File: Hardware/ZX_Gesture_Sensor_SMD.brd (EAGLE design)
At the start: 57.2 x 19.1 mm, 51 parts, among them Q1 MMBT2222A, Q2 MOSFET-NCHANNEL2N7002PW, U1 PIC16F1823-14PINTSSOP, U2 MCP6021T-E/OT, U3 DMC2700UDM, U4 DMC2700UDM, U5 TSOP57238TT1

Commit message: V04 changes
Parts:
- removed U$1: GESTURESENSE_LOGOSTEXT, SparkFun-Aesthetics:GESTURESENSE_TEXT
- moved R12 13.5 mm to (40.0, 9.21), turned to 0 degrees
- moved SJ2 12.3 mm to (40.1, 11.1), turned to 90 degrees
- moved R9 11.8 mm to (40.0, 13.0), turned to 180 degrees
- moved U$5 1.50 mm to (31.9, 8.47)
- moved LOGO1 1.27 mm to (26.4, -13.7)
- moved U$6 0.90 mm to (13.7, 6.86)
- moved FID4 0.50 mm to (51.3, 17.2)
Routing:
- net GND: track 128.8 -> 165.1 mm, vias 16 -> 12
- net I2C_ADDR: track 16.4 -> 31.5 mm
- net VCC: track 105.6 -> 109.0 mm, vias 6 -> 7
- net ICSPDAT/DACOUT: track 23.0 -> 26.1 mm
- net EM2: track 37.0 -> 39.8 mm
- net RECEIVER: track 21.1 -> 23.3 mm, vias 4 -> 2
- net MCLR: track 28.8 -> 30.1 mm
- net ICSPCLK/DATA_RDY: track 30.2 -> 31.5 mm
- added copper zone on layer 1, net N$26
- added copper zone on layer 16, net N$26
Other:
- board text added: "v04"
- board text removed: "v03"

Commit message: Updated Board File
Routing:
- net I2C_SDA: track 37.1 -> 38.2 mm
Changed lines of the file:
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@@
 <setting verticaltext="up"/>
 </settings>
-<grid distance="0.025" unitdist="inch" unit="inch" style="dots" multiple="1" display="yes" altdistance="0.005" altunitdist="inch" altunit="inch"/>
+<grid distance="0.0125" unitdist="inch" unit="inch" style="dots" multiple="1" display="yes" altdistance="0.005" altunitdist="inch" altunit="inch"/>
 <layers>
 <layer number="1" name="Top" color="4" fill="1" visible="yes" active="yes"/>
-<layer number="2" name="Route2" color="1" fill="3" visible="no" active="yes"/>
-<layer number="15" name="Route15" color="4" fill="6" visible="no" active="yes"/>
+<layer number="2" name="Route2" color="1" fill="3" visible="yes" active="yes"/>
+<layer number="15" name="Route15" color="4" fill="6" visible="yes" active="yes"/>
 <layer number="16" name="Bottom" color="1" fill="1" visible="yes" active="yes"/>
 <layer number="17" name="Pads" color="2" fill="1" visible="yes" active="yes"/>
@@
 <layer number="23" name="tOrigins" color="15" fill="1" visible="yes" active="yes"/>
 <layer number="24" name="bOrigins" color="15" fill="1" visible="yes" active="yes"/>
-<layer number="25" name="tNames" color="7" fill="1" visible="no" active="yes"/>
-<layer number="26" name="bNames" color="7" fill="1" visible="no" active="yes"/>
-<layer number="27" name="tValues" color="7" fill="1" visible="no" active="yes"/>
-<layer number="28" name="bValues" color="7" fill="1" visible="no" active="yes"/>
-<layer number="29" name="tStop" color="7" fill="3" visible="no" active="yes"/>
-<layer number="30" name="bStop" color="7" fill="6" visible="no" active="yes"/>
-<layer number="31" name="tCream" color="7" fill="4" visible="no" active="yes"/>
-<layer number="32" name="bCream" color="7" fill="5" visible="no" active="yes"/>
-<layer number="39" name="tKeepout" color="4" fill="11" visible="no" active="yes"/>
-<layer number="40" name="bKeepout" color="1" fill="11" visible="no" active="yes"/>
-<layer number="41" name="tRestrict" color="4" fill="10" visible="no" active="yes"/>
-<layer number="42" name="bRestrict" color="1" fill="10" visible="no" active="yes"/>
-<layer number="43" name="vRestrict" color="2" fill="10" visible="no" active="yes"/>
-<layer number="44" name="Drills" color="7" fill="1" visible="no" active="yes"/>
+<layer number="25" name="tNames" color="7" fill="1" visible="yes" active="yes"/>
+<layer number="26" name="bNames" color="7" fill="1" visible="yes" active="yes"/>
+<layer number="27" name="tValues" color="7" fill="1" visible="yes" active="yes"/>
+<layer number="28" name="bValues" color="7" fill="1" visible="yes" active="yes"/>
+<layer number="29" name="tStop" color="7" fill="3" visible="yes" active="yes"/>
+<layer number="30" name="bStop" color="7" fill="6" visible="yes" active="yes"/>
+<layer number="31" name="tCream" color="7" fill="4" visible="yes" active="yes"/>
+<layer number="32" name="bCream" color="7" fill="5" visible="yes" active="yes"/>
+<layer number="39" name="tKeepout" color="4" fill="11" visible="yes" active="yes"/>
+<layer number="40" name="bKeepout" color="1" fill="11" visible="yes" active="yes"/>
+<layer number="41" name="tRestrict" color="4" fill="10" visible="yes" active="yes"/>
+<layer number="42" name="bRestrict" color="1" fill="10" visible="yes" active="yes"/>
+<layer number="43" name="vRestrict" color="2" fill="10" visible="yes" active="yes"/>
+<layer number="44" name="Drills" color="7" fill="1" visible="yes" active="yes"/>
 <layer number="45" name="Holes" color="7" fill="1" visible="yes" active="yes"/>
-<layer number="46" name="Milling" color="3" fill="1" visible="no" active="yes"/>
-<layer number="47" name="Measures" color="7" fill="1" visible="no" active="yes"/>
+<layer number="46" name="Milling" color="3" fill="1" visible="yes" active="yes"/>
+<layer number="47" name="Measures" color="7" fill="1" visible="yes" active="yes"/>
 <layer number="51" name="tDocu" color="6" fill="1" visible="yes" active="yes"/>
-<layer number="52" name="bDocu" color="7" fill="1" visible="no" active="yes"/>
+<layer number="52" name="bDocu" color="7" fill="1" visible="yes" active="yes"/>
 <layer number="3" name="Route3" color="4" fill="3" visible="no" active="no"/>
 <layer number="4" name="Route4" color="1" fill="4" visible="no" active="no"/>
@@
 <text x="17.3228" y="2.2479" size="1.27" layer="21" font="vector" ratio="15" align="center-right">UART</text>
 <text x="40.7797" y="2.2479" size="1.27" layer="21" font="vector" ratio="15" align="center-left">I2C</text>
-<text x="42.34815" y="11.4681" size="0.8128" layer="22" font="vector" ratio="15" rot="MR270" align="bottom-center">I2C Addr</text>
+<text x="42.545" y="11.43" size="0.8128" layer="22" font="vector" ratio="15" rot="MR270" align="bottom-center">I2C Addr</text>
 <text x="23.5839" y="16.3195" size="1.778" layer="21" font="vector" ratio="15" align="bottom-center">ZX Gesture</text>
-<text x="53.6575" y="14.4145" size="1.2192" layer="16" font="vector" ratio="15" rot="R135" align="center">v04</text>
+<text x="53.6575" y="14.4145" size="1.016" layer="16" font="vector" ratio="15" rot="R115" align="center">v04</text>
 <text x="47.0535" y="6.985" size="0.8128" layer="22" font="vector" ratio="15" rot="MR0" align="bottom-center">I2C Pullups</text>
 <text x="18.4785" y="2.3495" size="0.8128" layer="21" font="vector" ratio="15" align="bottom-center">GRN</text>
@@
 <wire x1="32.385" y1="0" x2="32.385" y2="3.175" width="0.2032" layer="21"/>
 <wire x1="32.385" y1="3.175" x2="32.385" y2="0" width="0.2032" layer="22"/>
-<text x="38.6715" y="13.49375" size="0.8128" layer="22" font="vector" ratio="15" rot="MR270">O: 0x20
+<text x="38.4175" y="13.6525" size="0.8128" layer="22" font="vector" ratio="15" rot="MR270">O: 0x20
 C: 0x22</text>
 <wire x1="11.938" y1="8.128" x2="11.938" y2="10.922" width="0.2032" layer="21"/>
@@
 <wire x1="51.91125" y1="6.73735" x2="51.9938" y2="6.6548" width="0.2032" layer="16"/>
 <wire x1="51.855" y1="8.675" x2="51.91125" y2="8.73125" width="0.2032" layer="16"/>
-<via x="28.575" y="5.715" extent="1-16" drill="0.508"/>
+<via x="28.575" y="5.715" extent="1-16" drill="0.381"/>
 <polygon width="0.2032" layer="1" isolate="0.3048">
 <vertex x="26.035" y="19.05"/>
@@
 <via x="22.5425" y="4.445" extent="1-16" drill="0.381"/>
 <via x="38.735" y="3.81" extent="1-16" drill="0.381"/>
-<wire x1="45.085" y1="3.81" x2="38.735" y2="3.81" width="0.2032" layer="16"/>
-<wire x1="45.085" y1="4.23" x2="45.085" y2="3.81" width="0.2032" layer="16"/>
 <wire x1="19.655" y1="11.3633" x2="19.655" y2="9.2375" width="0.2032" layer="16"/>
 <wire x1="23.1775" y1="8.89" x2="23.1775" y2="5.08" width="0.2032" layer="1"/>
@@
 <wire x1="38.4175" y1="4.1275" x2="38.735" y2="3.81" width="0.2032" layer="16"/>
 <wire x1="24.4475" y1="3.81" x2="33.655" y2="3.81" width="0.2032" layer="16"/>
+<wire x1="45.085" y1="4.23" x2="45.085" y2="3.175" width="0.2032" layer="16"/>
+<wire x1="45.085" y1="3.175" x2="44.7675" y2="2.8575" width="0.2032" layer="16"/>
+<wire x1="44.7675" y1="2.8575" x2="39.6875" y2="2.8575" width="0.2032" layer="16"/>
+<wire x1="39.6875" y1="2.8575" x2="38.735" y2="3.81" width="0.2032" layer="16"/>
 </signal>
 <signal name="I2C_SCL">
@@
 <wire x1="23.8125" y1="9.8425" x2="24.13" y2="9.525" width="0.2032" layer="16"/>
 <wire x1="36.068" y1="3.302" x2="36.957" y2="3.302" width="0.2032" layer="16"/>
-<wire x1="43.815" y1="4.7625" x2="38.4175" y2="4.7625" width="0.254" layer="16"/>
-<wire x1="38.4175" y1="4.7625" x2="38.1" y2="5.08" width="0.254" layer="16"/>
-<via x="38.1" y="5.08" extent="1-16" drill="0.508"/>
-<via x="37.211" y="3.048" extent="1-16" drill="0.508"/>
-<wire x1="37.211" y1="3.048" x2="37.211" y2="4.191" width="0.254" layer="1"/>
-<wire x1="37.211" y1="4.191" x2="38.1" y2="5.08" width="0.254" layer="1"/>
+<wire x1="43.815" y1="4.7625" x2="38.4175" y2="4.7625" width="0.2032" layer="16"/>
+<wire x1="38.4175" y1="4.7625" x2="38.1" y2="5.08" width="0.2032" layer="16"/>
+<via x="38.1" y="5.08" extent="1-16" drill="0.381"/>
+<via x="37.211" y="3.048" extent="1-16" drill="0.381"/>
+<wire x1="37.211" y1="3.048" x2="37.211" y2="4.191" width="0.2032" layer="1"/>
+<wire x1="37.211" y1="4.191" x2="38.1" y2="5.08" width="0.2032" layer="1"/>
 <wire x1="36.957" y1="3.302" x2="37.211" y2="3.048" width="0.2032" layer="16"/>
 <wire x1="36.195" y1="1.27" x2="36.195" y2="3.175" width="0.2032" layer="16"/>

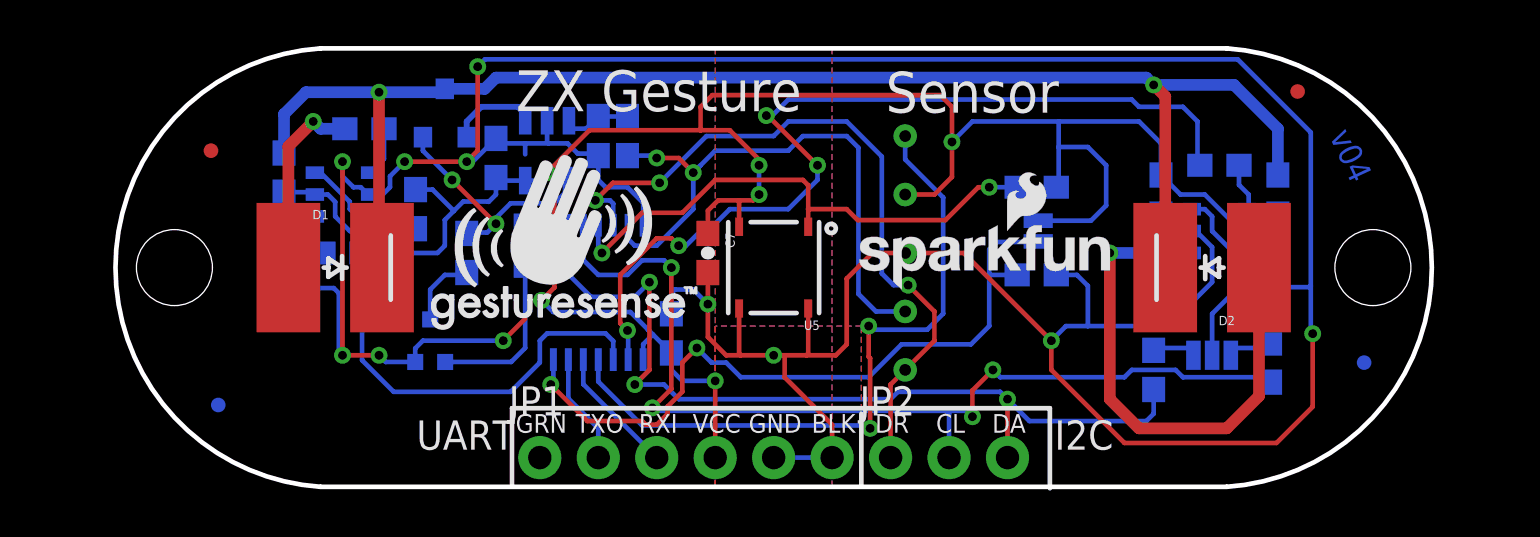
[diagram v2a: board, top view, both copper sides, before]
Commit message: Updated Brd File per Engineering Design Review
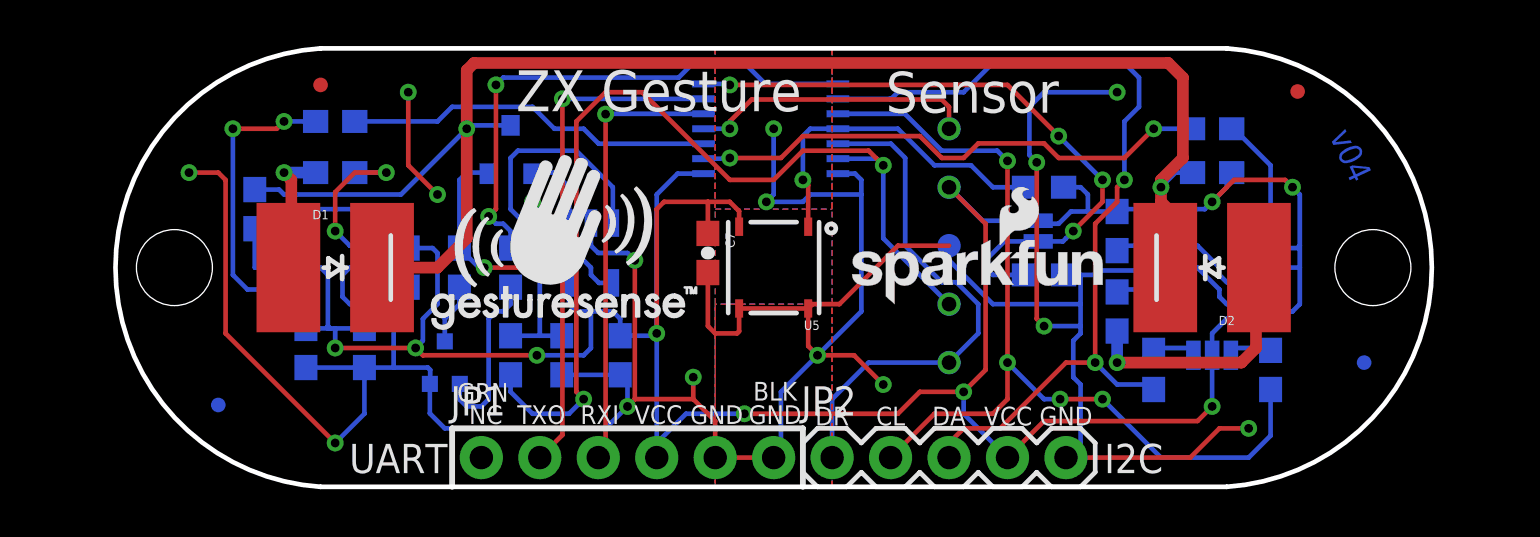
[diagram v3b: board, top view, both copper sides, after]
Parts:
- JP2: device SparkFun-Connectors:1X03_NO_SILK -> SparkFun-Connectors:1X05
- moved R1 10.8 mm to (17.1, 5.71)
- moved U1 10.3 mm to (28.4, 15.6), turned to 90 degrees
- moved C1 10.0 mm to (10.8, 6.03), turned to 270 degrees
- moved R2 9.66 mm to (19.4, 5.71)
- moved R13 5.72 mm to (9.53, 15.9)
- moved FID3 5.55 mm to (8.89, 17.5)
- moved U2 4.84 mm to (20.6, 10.2)
- moved C3 4.55 mm to (8.26, 6.03)
- moved Q1 3.27 mm to (17.1, 14.6)
- moved U3 3.19 mm to (9.53, 9.53)
- moved C6 3.01 mm to (47.6, 13.7), turned to 180 degrees
- moved R8 2.69 mm to (43.5, 7.62), turned to 270 degrees
- moved R5 2.56 mm to (12.7, 9.53)
- moved JP2 2.54 mm to (31.1, 1.27)
- moved JP1 2.54 mm to (15.9, 1.27)
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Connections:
- net GND: now also JP2.5
- net VCC: now also JP2.4
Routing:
- net VCC: track 109.0 -> 135.7 mm, vias 7 -> 10
- net CARRIER: track 1.24 -> 23.4 mm, vias 0 -> 2
- net MCLR: track 30.1 -> 12.5 mm, vias 3 -> 2
- net UART_RX: track 4.80 -> 22.1 mm, vias 0 -> 1
- net EM2: track 39.8 -> 23.1 mm, vias 4 -> 2
- net ICSPDAT/DACOUT: track 26.1 -> 42.8 mm
- net N$1: track 3.11 -> 17.3 mm
- net UART_TX: track 5.58 -> 19.3 mm, vias 0 -> 1
- net N$15: track 1.73 -> 13.6 mm, vias 0 -> 2
- net N$12: track 21.8 -> 11.3 mm
- net ICSPCLK/DATA_RDY: track 31.5 -> 22.6 mm, vias 4 -> 1
- net RECEIVER: track 23.3 -> 14.8 mm, vias 2 -> 1
- net N$8: track 5.57 -> 11.6 mm
- net N$6: track 2.16 -> 7.10 mm, vias 0 -> 2
- net N$2: track 11.2 -> 16.1 mm
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- removed copper zone on layer 1, net N$26
- removed copper zone on layer 16, net N$26
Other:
- board text added: "NC"

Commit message: Updated Brd/Sch files per QC Review
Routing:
- net GND: track 162.5 -> 163.7 mm, vias 15 -> 16
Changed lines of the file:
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@@
 <setting verticaltext="up"/>
 </settings>
-<grid distance="0.1" unitdist="inch" unit="inch" style="dots" multiple="1" display="yes" altdistance="0.005" altunitdist="inch" altunit="inch"/>
+<grid distance="0.0125" unitdist="inch" unit="inch" style="dots" multiple="1" display="yes" altdistance="0.005" altunitdist="inch" altunit="inch"/>
 <layers>
-<layer number="1" name="Top" color="4" fill="1" visible="yes" active="yes"/>
+<layer number="1" name="Top" color="4" fill="1" visible="no" active="yes"/>
 <layer number="2" name="Route2" color="1" fill="3" visible="no" active="yes"/>
 <layer number="15" name="Route15" color="4" fill="6" visible="no" active="yes"/>
@@
 <layer number="43" name="vRestrict" color="2" fill="10" visible="no" active="yes"/>
 <layer number="44" name="Drills" color="7" fill="1" visible="no" active="yes"/>
-<layer number="45" name="Holes" color="7" fill="1" visible="yes" active="yes"/>
+<layer number="45" name="Holes" color="7" fill="1" visible="no" active="yes"/>
 <layer number="46" name="Milling" color="3" fill="1" visible="no" active="yes"/>
 <layer number="47" name="Measures" color="7" fill="1" visible="no" active="yes"/>
-<layer number="51" name="tDocu" color="6" fill="1" visible="yes" active="yes"/>
+<layer number="51" name="tDocu" color="6" fill="1" visible="no" active="yes"/>
 <layer number="52" name="bDocu" color="7" fill="1" visible="no" active="yes"/>
 <layer number="3" name="Route3" color="4" fill="3" visible="no" active="no"/>
@@
 <layer number="112" name="tSilk" color="7" fill="1" visible="no" active="no"/>
 <layer number="113" name="IDFDebug" color="7" fill="1" visible="no" active="no"/>
-<layer number="114" name="Badge_Outline" color="7" fill="1" visible="yes" active="yes"/>
-<layer number="115" name="ReferenceISLANDS" color="7" fill="1" visible="yes" active="yes"/>
+<layer number="114" name="Badge_Outline" color="7" fill="1" visible="no" active="yes"/>
+<layer number="115" name="ReferenceISLANDS" color="7" fill="1" visible="no" active="yes"/>
 <layer number="116" name="Patch_BOT" color="9" fill="4" visible="no" active="no"/>
-<layer number="118" name="Rect_Pads" color="7" fill="1" visible="yes" active="yes"/>
+<layer number="118" name="Rect_Pads" color="7" fill="1" visible="no" active="yes"/>
 <layer number="121" name="_tsilk" color="7" fill="1" visible="no" active="no"/>
 <layer number="122" name="_bsilk" color="7" fill="1" visible="no" active="no"/>
@@
 <wire x1="28.8925" y1="4.1275" x2="28.8925" y2="1.5875" width="0.2032" layer="16"/>
 <wire x1="28.8925" y1="1.5875" x2="28.575" y2="1.27" width="0.2032" layer="16"/>
-<wire x1="36.195" y1="10.4775" x2="33.9725" y2="10.4775" width="0.2032" layer="1"/>
-<wire x1="33.9725" y1="10.4775" x2="31.4325" y2="7.9375" width="0.2032" layer="1"/>
-<wire x1="31.4325" y1="7.9375" x2="30.2625" y2="7.9375" width="0.2032" layer="1"/>
-<wire x1="30.2625" y1="7.9375" x2="30.075" y2="7.75" width="0.2032" layer="1"/>
 <wire x1="30.075" y1="7.75" x2="30.075" y2="6.12" width="0.2032" layer="1"/>
 <wire x1="30.075" y1="6.12" x2="30.48" y2="5.715" width="0.2032" layer="1"/>
@@
 <wire x1="41.91" y1="4.445" x2="41.91" y2="1.905" width="0.2032" layer="16"/>
 <contactref element="TP3" pad="P$1"/>
-<wire x1="36.195" y1="10.4775" x2="36.195" y2="10.4775" width="0" layer="19" extent="1-16"/>
+<via x="36.195" y="10.4775" extent="1-16" drill="0.635"/>
+<wire x1="36.195" y1="10.4775" x2="36.195" y2="9.8425" width="0.2032" layer="16"/>
+<wire x1="36.195" y1="10.4775" x2="35.2425" y2="10.4775" width="0.2032" layer="1"/>
+<wire x1="35.2425" y1="10.4775" x2="33.3375" y2="8.5725" width="0.2032" layer="1"/>
+<wire x1="33.3375" y1="8.5725" x2="33.3375" y2="4.445" width="0.2032" layer="1"/>
 </signal>
 <signal name="I2C_SDA">

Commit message: Updated SCH & BRD Files
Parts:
- R3: value 10 -> 1K 1%
- U5: value TSOP57238TT1 -> TSSP57038
- moved TP1 15.3 mm to (21.0, 16.8)
- moved TP2 13.3 mm to (23.5, 16.8)
- moved TP5 12.5 mm to (31.1, 16.8)
- moved TP3 12.0 mm to (26.0, 16.8)
- moved TP4 11.7 mm to (28.6, 16.8)
- moved R1 11.4 mm to (28.6, 5.71), turned to 0 degrees
- moved R13 11.0 mm to (20.3, 14.0)
- moved U1 6.03 mm to (28.6, 9.53)
- moved FID3 5.93 mm to (3.17, 15.9)
- moved C4 5.85 mm to (7.30, 6.35)
- moved FID4 3.27 mm to (54.2, 15.6)
- moved FID1 2.31 mm to (2.22, 4.19)
- moved Q1 1.99 mm to (15.4, 13.7)
- moved U$6 1.69 mm to (14.8, 5.59)
- moved JP1 1.42 mm to (16.5, 2.54)
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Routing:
- net GND: track 163.7 -> 73.5 mm, vias 16 -> 19
- net ICSPDAT/DACOUT: track 42.8 -> 18.2 mm, vias 3 -> 1
- net N$15: track 13.6 -> 35.2 mm
- net EM2: track 23.1 -> 37.5 mm
- net I2C_SDA: track 38.8 -> 27.4 mm, vias 2 -> 3
- net I2C_SCL: track 40.4 -> 31.7 mm, vias 4 -> 3
- net UART_TX: track 19.3 -> 10.8 mm
- net ICSPCLK/DATA_RDY: track 22.6 -> 30.7 mm, vias 1 -> 5
- net UART_RX: track 22.1 -> 14.7 mm
- net N$2: track 16.1 -> 9.48 mm
- net EM1: track 16.1 -> 9.55 mm
- net N$6: track 7.10 -> 1.73 mm, vias 2 -> 0
- net COMMON: track 66.0 -> 60.8 mm, vias 2 -> 3
- net N$8: track 11.6 -> 6.58 mm
- net I2C_ADDR: track 28.3 -> 23.5 mm
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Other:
- board size 57.2 x 19.1 mm -> 62.4 x 16.5 mm

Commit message: Updated BRD and SCH files
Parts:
- moved TP1 2.86 mm to (23.8, 16.8)
- moved TP2 2.54 mm to (26.0, 16.8)
- moved TP3 2.22 mm to (28.3, 16.8)
- moved TP4 1.91 mm to (30.5, 16.8)
- moved TP5 1.59 mm to (32.7, 16.8)
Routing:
- net VCC: track 134.5 -> 137.8 mm
- net ICSPCLK/DATA_RDY: track 30.7 -> 29.1 mm
- net MCLR: track 10.9 -> 9.70 mm
- net N$5: track 6.31 -> 5.57 mm
- net N$1: track 20.7 -> 21.3 mm
- net GND: track 73.5 -> 73.8 mm, vias 19 -> 24
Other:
- outline, holes or cut-outs redrawn
- board text added: "v05"
- board text removed: "v04"

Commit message: updated BRD Files
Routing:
- net GND: track 73.8 -> 72.1 mm
